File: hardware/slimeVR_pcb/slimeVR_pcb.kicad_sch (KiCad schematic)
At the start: 58 parts, among them J1 HRO_TYPE-C-31-M-12, Q1 8205A, SW1 SK12D07VG4, SW2 SW_Push, U1 ESP32-S2-WROVER, U10 AP2112K-3.3, U2 TP4057, U3 ICM-45686, U4 FUSB302BUCX, U5 QMC6309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

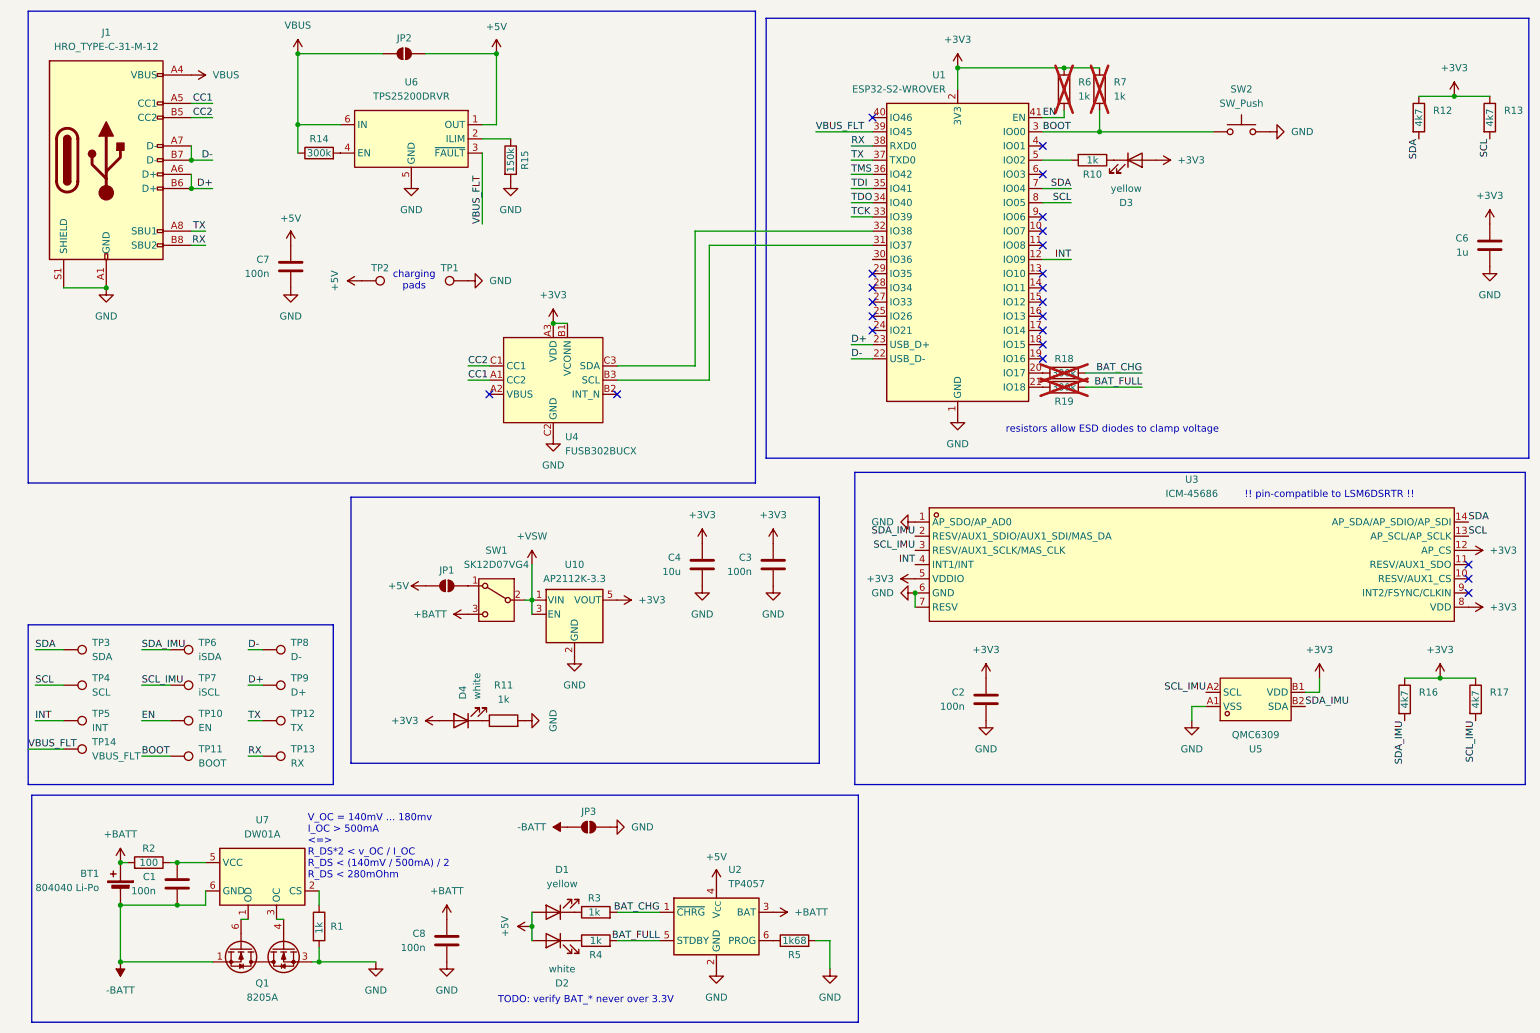
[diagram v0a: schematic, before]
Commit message: give up on FUSB302 idea i need to supply power via USB C safely, without adding more comonents i need 2 datalines for i2c i could detect shorting of sbu 1 and sbu 2, then use the CC or D+/D- pins for i2c comms
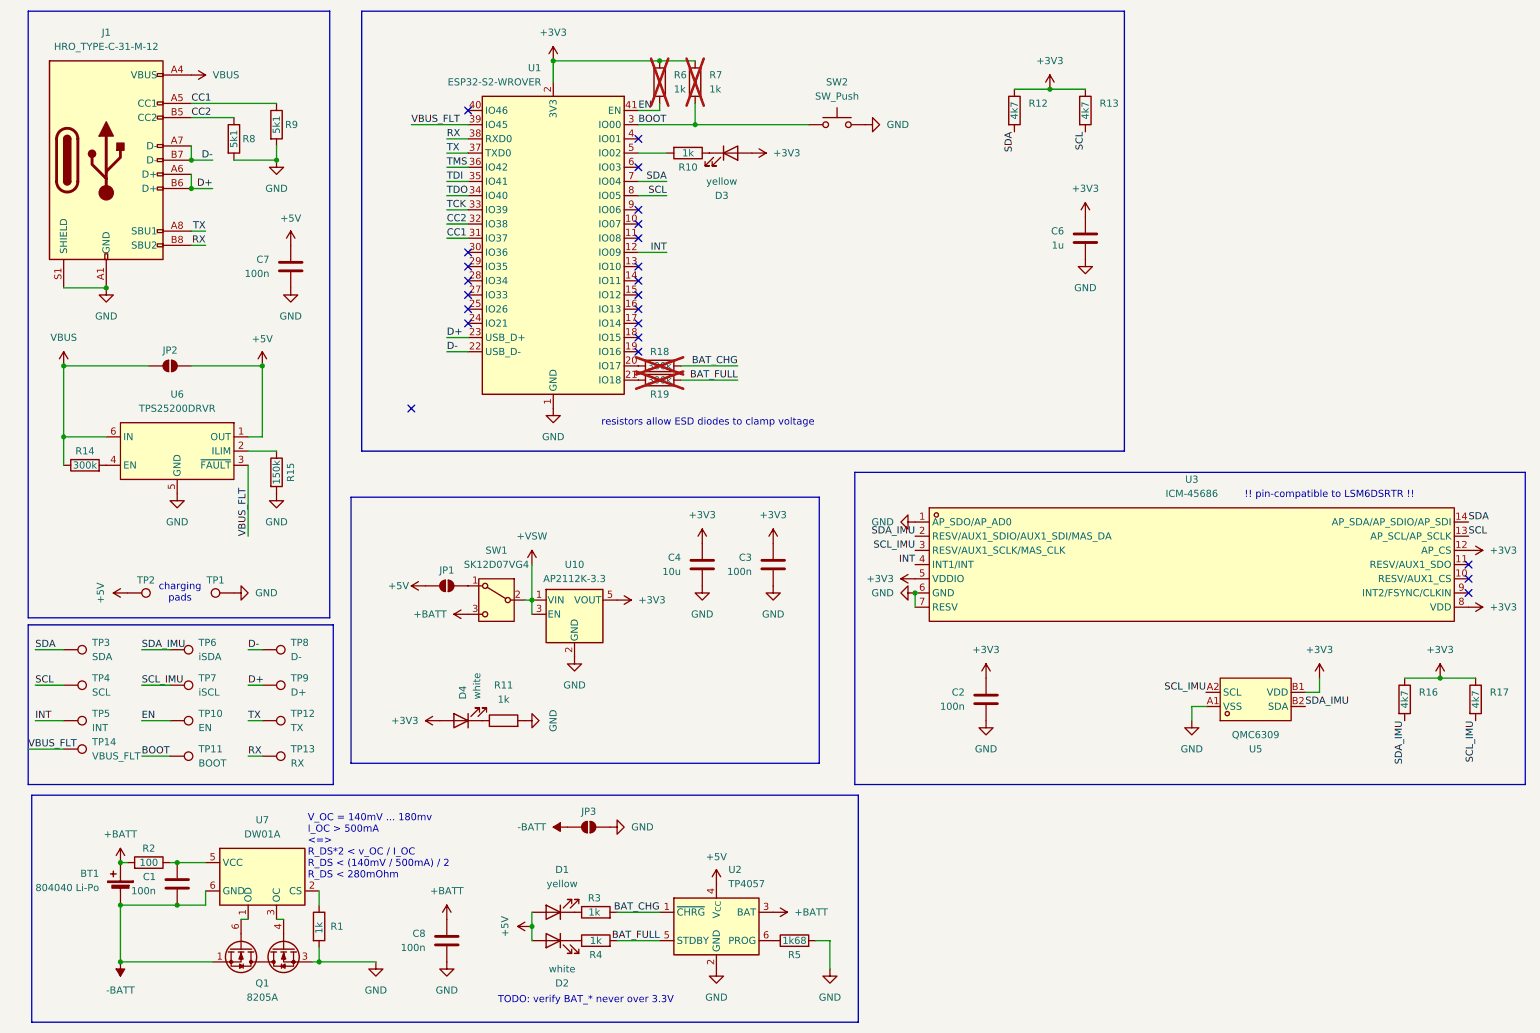
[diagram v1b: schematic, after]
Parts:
- removed U4: FUSB302BUCX, easyeda2kicad:WLCSP-9_L1.3-W1.2-R3-C3-P0.40-TL, symbol slime_parts:FUSB302BUCX
- added R8, R9: 5k1, Resistor_SMD:R_0603_1608Metric_Pad0.98x0.95mm_HandSolder, symbol Device:R
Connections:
- net CC1: now also U1.31 (IO37), R9.1
- net CC2: now also U1.32 (IO38), R8.1
- net GND: now also R8.2, R9.2
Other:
- moved on the sheet: C6, D3, JP2, R10, R12, R13, R14, R15, R18, R19, R6, R7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

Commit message: fix typo
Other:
- title: (none) -> Slimeinator
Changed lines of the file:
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@@
 	(generator_version "9.0")
 	(paper "A4")
+	(title_block
+		(title "Slimeinator")
+		(rev "v0")
+		(comment 1 "Schematic & Layout: H3")
+		(comment 2 "Project: LilyFox, H3, Eleos")
+	)
 	(rectangle
 		(start 15.24 123.825)

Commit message: fixup partsel, fixup silkscreen
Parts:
- D1, D3: LCSC C2296 -> C2296
- D4: LCSC C2290 -> C34499; LCSC Part C2290 -> (none)
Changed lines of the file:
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@@
 			)
 		)
-		(property "LCSC Part" "C2290"
-			(at 92.71 140.97 90)
-			(effects
-				(font
-					(size 1.27 1.27)
-				)
-				(hide yes)
-			)
-		)
-		(property "LCSC" "C2290"
+		(property "LCSC" "C34499"
 			(at 93.0274 137.16 0)
 			(effects
@@
 			)
 		)
-		(property "LCSC" " C2296"
+		(property "LCSC" "C2296"
 			(at 110.8075 167.64 0)
 			(effects
@@
 			)
 		)
-		(property "LCSC" " C2296"
+		(property "LCSC" "C2296"
 			(at 139.3825 46.99 0)
 			(effects

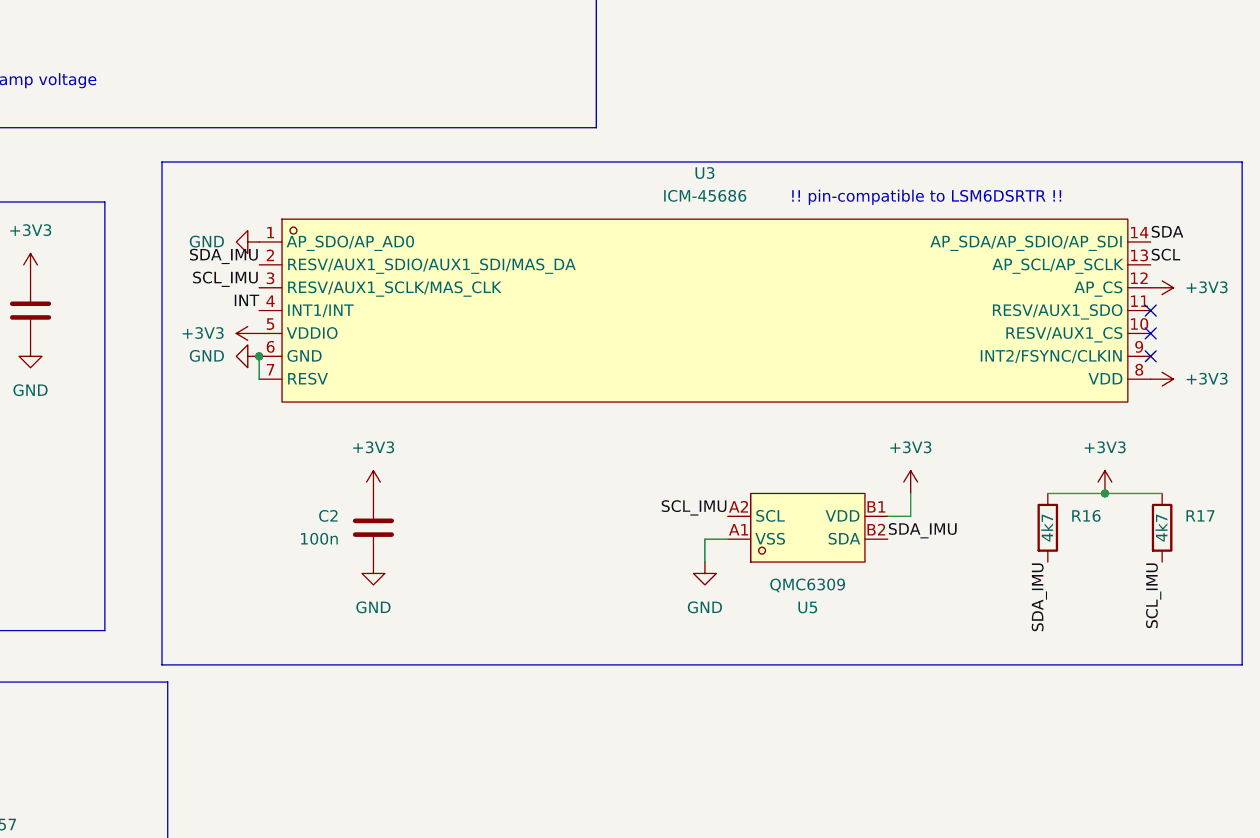
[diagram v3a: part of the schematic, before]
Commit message: add oscillator for IMU
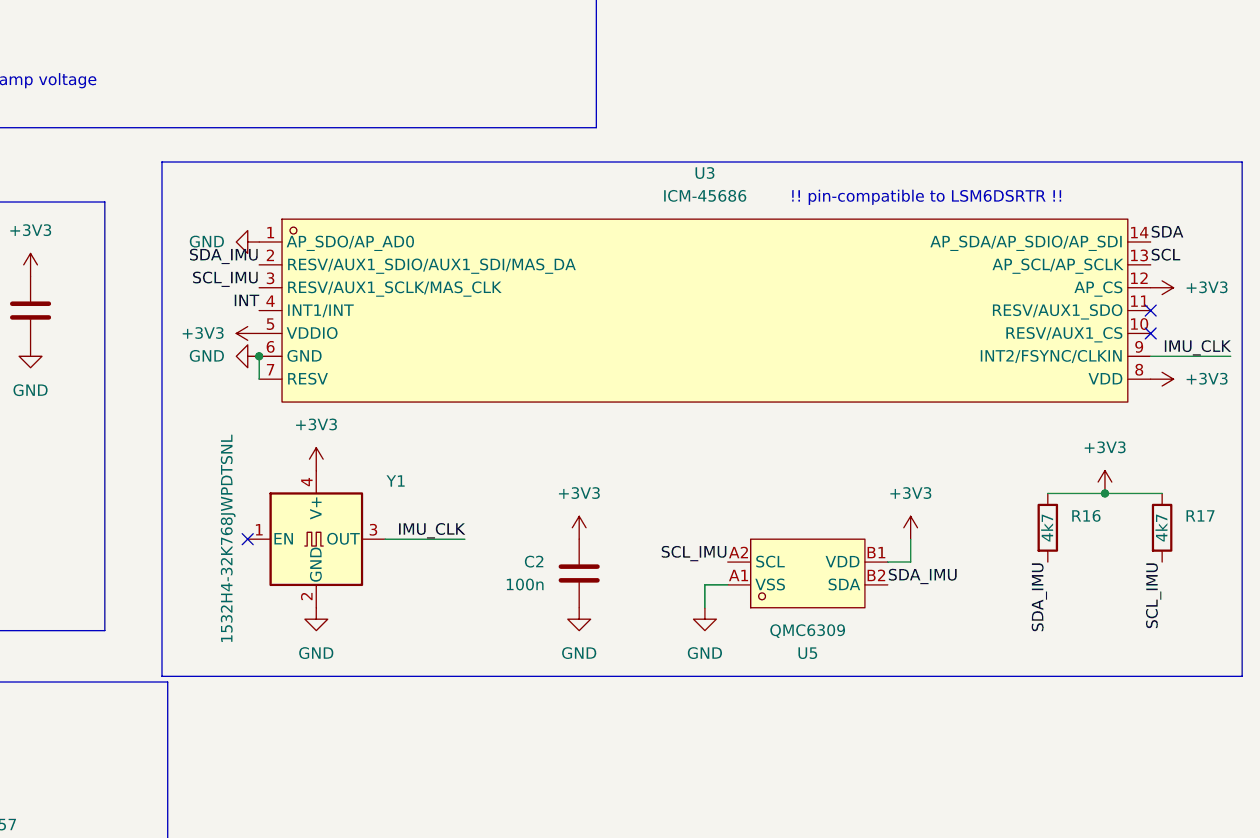
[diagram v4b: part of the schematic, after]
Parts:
- added Y1: 1532H4-32K768JWPDTSNL, Oscillator:Oscillator_SMD_EuroQuartz_XO32-4Pin_3.2x2.5mm, symbol Oscillator:XO32
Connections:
- net +3V3: now also Y1.4 (V+)
- net GND: now also Y1.2 (GND)
- net IMU_CLK: now reaches U3.9 (INT2/FSYNC/CLKIN)
- net IMU_CLK: now also Y1.3 (OUT)
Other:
- moved on the sheet: C2, U5

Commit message: fix osc footprint
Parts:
- Y1: footprint Oscillator:Oscillator_SMD_EuroQuartz_XO32-4Pin_3.2x2.5mm -> easyeda2kicad:OSC-SMD_4P-L3.2-W2.5-CJ13-320001210A20
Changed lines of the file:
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@@
 			)
 		)
-		(property "Footprint" "Oscillator:Oscillator_SMD_EuroQuartz_XO32-4Pin_3.2x2.5mm"
+		(property "Footprint" "easyeda2kicad:OSC-SMD_4P-L3.2-W2.5-CJ13-320001210A20"
 			(at 198.12 147.32 0)
 			(effects

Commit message: silk n stuff
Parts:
- added C5: 100n, Capacitor_SMD:C_0603_1608Metric_Pad1.08x0.95mm_HandSolder, symbol Device:C
- added R20, R21: 1k, Resistor_SMD:R_0603_1608Metric_Pad0.98x0.95mm_HandSolder, symbol Device:R
- added TP15: iCLK, TestPoint:TestPoint_Pad_D1.0mm, symbol Connector:TestPoint
- TP3: value SDA -> µSDA
- TP4: value SCL -> µSCL
- TP5: value INT -> µINT
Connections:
- net +VSW: now also C5.1, R21.1
- net GND: now also C5.2, R20.2
- net IMU_CLK: now also TP15.1
- net BAT_SENSE: now reaches U1.4 (IO01)
- net BAT_SENSE: now also R20.1, R21.2
- no-connect marks 23 -> 22
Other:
- moved on the sheet: D4, R11
